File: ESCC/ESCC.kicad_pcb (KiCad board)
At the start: 2 copper layers, 23 parts, among them J1 Conn_01x03, J2 Conn_01x05, J3 SWD_UART, U1 STM32F072CBUx, U2 AZ1117-3.3, U3 ATA6561, U4 BESC

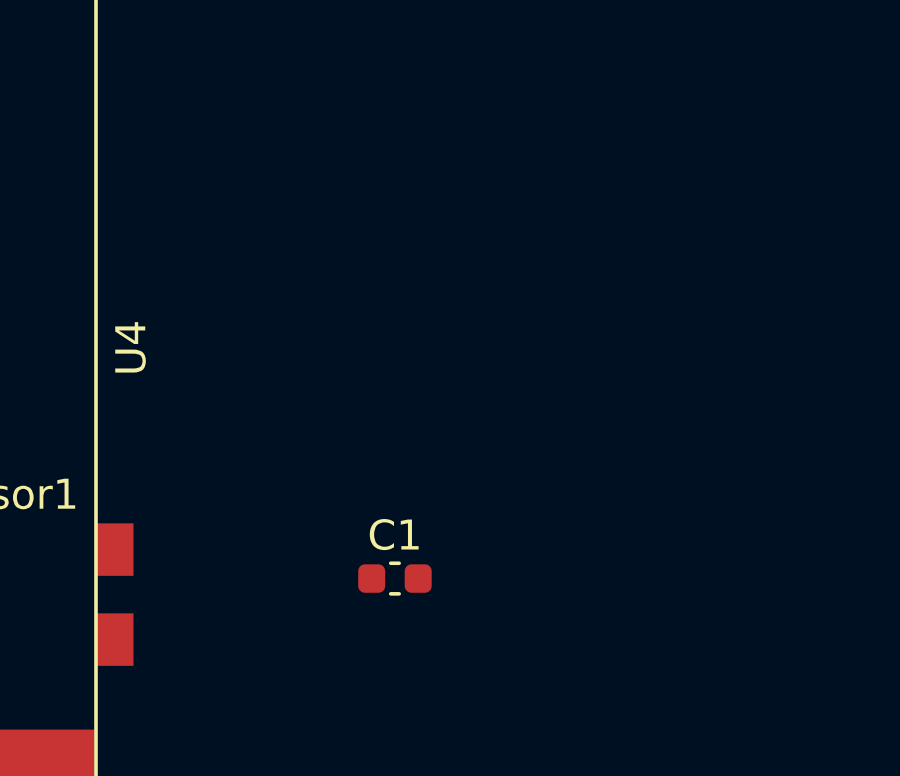
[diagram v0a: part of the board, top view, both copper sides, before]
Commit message: Assigned footprints to schematic
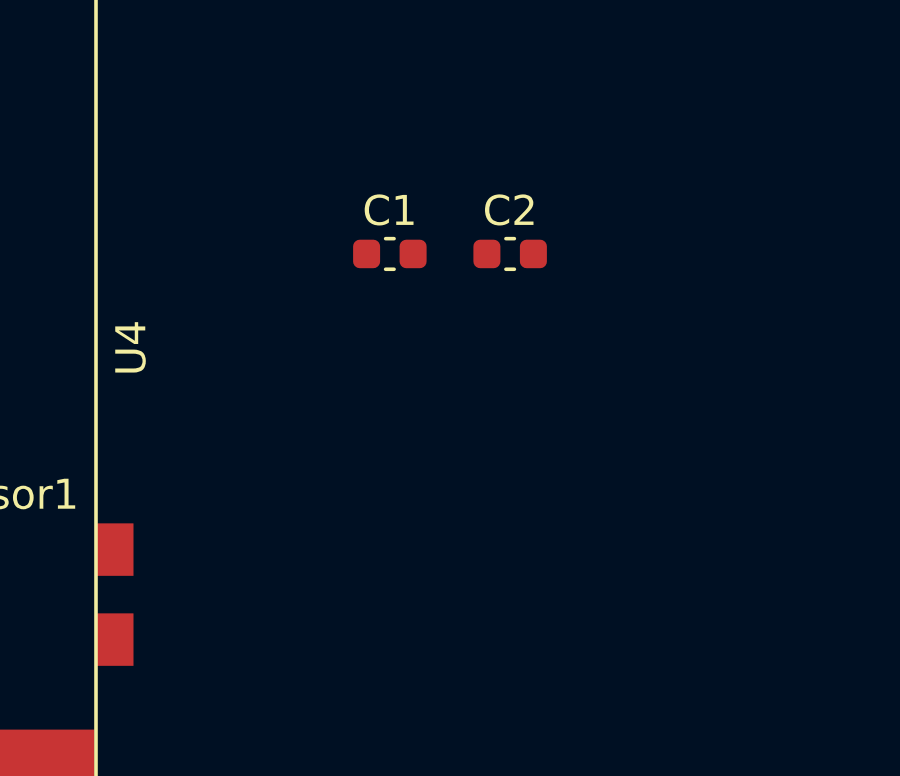
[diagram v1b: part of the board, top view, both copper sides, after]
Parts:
- added C2: DNP, Capacitor_SMD:C_0603_1608Metric, F.Cu at (145.0, 83.8)
- C1: value 100 nF -> 100n
- moved C1 10.8 mm to (141.0, 83.8)
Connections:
- C1 pad 1: +12V -> GND
- C1 pad 2: GND -> +3V3

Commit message: Finished ESCC layout
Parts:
- removed 30A_Current_Sensor1: ACS725xLCTR-30AB, Package_SO:SOIC-8_3.9x4.9mm_P1.27mm
- added D1: LED, LED_SMD:LED_0603_1608Metric, B.Cu at (150.5, 83.2)
- added R1: 150, Resistor_SMD:R_0603_1608Metric, B.Cu at (152.0, 83.2)
- added SW1: RST, Button_Switch_SMD:SW_SPST_PTS810, B.Cu at (144.8, 89.5)
- added SW2: DBG, Button_Switch_SMD:SW_SPST_PTS810, B.Cu at (155.8, 83.2)
- added U5: ACS725xLCTR-30AB, Package_SO:SOIC-8_3.9x4.9mm_P1.27mm, B.Cu at (163.5, 106.5)
- C1, C10, C11, C12, C13, C14, C15, C16, C2, C4, C5, C6, C7, C8, C9, J3, R4, U1, U2, U3: moved to B.Cu
- moved C13 64.7 mm to (147.0, 107.8), turned to 180 degrees
- moved R4 48.3 mm to (150.0, 91.0), turned to 90 degrees
- moved C4 47.5 mm to (154.2, 86.8), turned to 90 degrees
- moved J1 42.6 mm to (148.2, 85.2), turned to 90 degrees
- moved C11 41.2 mm to (151.5, 86.0), turned to 180 degrees
- moved C5 40.1 mm to (151.5, 99.0)
- moved C9 39.6 mm to (156.5, 86.0), turned to 180 degrees
- moved C6 38.5 mm to (151.5, 97.5)
- moved C12 36.7 mm to (151.5, 87.5), turned to 180 degrees
- moved C10 35.7 mm to (156.5, 87.5), turned to 180 degrees
- moved U1 35.1 mm to (155.0, 92.5), turned to 270 degrees
- moved J3 32.3 mm to (144.8, 95.2)
- moved U4 31.8 mm to (151.5, 100.0), turned to 0 degrees
- moved C8 31.3 mm to (158.5, 97.5)
- moved C7 28.8 mm to (158.5, 99.0)
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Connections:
- net /DBG2 renamed /NOGGIN/PF1
- net /LED_B renamed /NOGGIN/PC15
- net /LED_G renamed /NOGGIN/PC14
- J2 pad : (no net) -> GND
- J2 pad 2: GND -> +5V
- J2 pad 3: +5V -> GND
- U1 pad 14: /ESC_SIG -> /NOGGIN/PA4(DAC1)
- U1 pad 16: /CURR_OUT -> /NOGGIN/PA6
- U1 pad 17: /NOGGIN/PA7 -> /CURR_OUT
- U1 pad 2: /LED_R -> /LED
- U1 pad 40: /NOGGIN/PB4 -> /ESC_SIG
- U1 pad 5: /DBG1 -> /DBG
- U4 pad 4: Net-(30A_Current_Sensor1-Pad1) -> /12V_SENSED
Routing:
- net +3V3: track 0.00 -> 72.4 mm, vias 0 -> 4
- net /ESC_SIG: track 0.00 -> 28.4 mm, vias 0 -> 1
- net /CURR_OUT: track 0.00 -> 20.2 mm
- net /RST: track 0.00 -> 19.3 mm, vias 0 -> 2
- net GND: track 0.40 -> 16.9 mm, vias 0 -> 34
- net +5V: track 0.00 -> 15.9 mm, vias 0 -> 1
- net /NOGGIN/PA10(UART_RX): track 0.00 -> 15.7 mm, vias 0 -> 2
- net /CAN_TX: track 0.00 -> 11.4 mm
- net /NOGGIN/PA9(UART_TX): track 0.00 -> 10.6 mm, vias 0 -> 2
- net /DBG: track 0.00 -> 9.23 mm
- net /NOGGIN/SWDIO: track 0.00 -> 8.38 mm, vias 0 -> 2
- net /CAN_RX: track 0.00 -> 7.36 mm
- net Net-(J1-Pad1): track 6.91 -> 0.00 mm, vias 0 -> 21
- net Net-(J1-Pad3): track 5.95 -> 0.00 mm, vias 0 -> 12
- net /LED: track 0.00 -> 5.51 mm
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- added copper zone on B.Cu, net +12V
- added copper zone on F.Cu, net +12V
- added copper zone on B.Cu, net /12V_SENSED
- added copper zone on F.Cu, net /12V_SENSED
- added copper zone on B.Cu, net GND
- added copper zone on F.Cu, net GND
- added copper zone on B.Cu, net Net-(J1-Pad1)
- added copper zone on F.Cu, net Net-(J1-Pad1)
- added copper zone on B.Cu, net Net-(J1-Pad2)
- added copper zone on F.Cu, net Net-(J1-Pad2)
- added copper zone on B.Cu, net Net-(J1-Pad3)
- added copper zone on F.Cu, net Net-(J1-Pad3)
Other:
- board outline added: 36 x 40 mm
- board text added: "ESCC v1 Kaushik Prakash Matthew Tran"
